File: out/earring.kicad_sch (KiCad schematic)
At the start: 51 parts, among them J1 USB-C, SW1 BOOTSEL, SW2 PWR, U1 RP2350A, U2 LGS4056H, U3 NCP730-3.3, U4 TPS22913, U5 USBLC6-2P6, U6 LSM6DS3TR-C, U7 W25Q16JVUXIQ, Y1 12MHz

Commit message: Link schematic to PCB: footprint properties, UUID paths, fp-lib-table
Fixes 'Cannot update <ref> (no footprint assigned)' on Update PCB from
Schematic. Four things were missing:

- Symbols had no Footprint property. Each now carries
  'earring:<footprint>' taken from bom/parts.yaml via circuit.py.
- No fp-lib-table, so that nickname resolved to nothing. gen_board.py
  writes out/fp-lib-table pointing at library/parts.pretty (tracked).
- Board footprints had bare FPIDs and empty paths, so KiCad could not
  tell that board R10 IS schematic R10. gen_board.py now stamps the
  library nickname and the schematic symbol's UUID path; both sides
  derive UUIDs deterministically, so neither has to run first.
- The project file listed no root sheet ('sheets': []).

The bigger fix: the schematic is now COMPLETE. The 45-LED chain and the
bypass-cap banks were collapsed to representatives plus a note, which
reads well but is wrong for a sheet that drives the board — KiCad
offers to DELETE any footprint with no matching symbol, so the 41
undrawn LEDs and 23 ring caps were at risk. They are drawn in full as
grids (page A2 -> A1), with an assert that every component is placed.
Unused pins get no-connect flags instead of dangling.

The existing PARTIAL board was patched in place, NOT regenerated:
1363 tracks before and after, DRC unchanged at 0 errors / 8 unconnected.

Verified: kicad-cli sch erc = 0 violations; netlist export = 122/122
components with footprints; cross-check of every board footprint
against its symbol = 0 path/footprint/orphan mismatches.

Co-Authored-By: Claude Fable 5 <noreply@anthropic.com>
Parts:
- added C2, C3, C30, C32, C34, C36, C38, C4, C40, C42, C44, C46, C48, C5, C50, C52, C54, C56, C58, C6, C60, C62, C64, C66, C68, C7, C70, C72, C74, C8: 100n, earring:C_0402_1005Metric, symbol gen:c_100n
- added LED10, LED11, LED12, LED13, LED14, LED15, LED16, LED17, LED18, LED19, LED20, LED21, LED22, LED23, LED24, LED25, LED26, LED27, LED28, LED29, LED3, LED30, LED31, LED32, LED33, LED34, LED35, LED36, LED37, LED38, LED39, LED4, LED40, LED41, LED42, LED43, LED5, LED6, LED7, LED8, LED9: SK6805-EC10, earring:LED_SK6805-EC10, symbol gen:led
- BT1: footprint (none) -> earring:BAT_CR2032_W
- C1, C14, C15, C18, C19, C21, C23, C24, C25, C9: footprint (none) -> earring:C_0402_1005Metric
- C11, C12, C13, C22: footprint (none) -> earring:C_0402_1005Metric_small_pads
- C16, C17, C20: footprint (none) -> earring:C_0603_1608Metric
- J1: footprint (none) -> earring:USB-C_SMD-TYPE-C-31-M-12_1
- L1: footprint (none) -> earring:L_pol_2016
- LED1, LED2, LED44, LED45: footprint (none) -> earring:LED_SK6805-EC10
- R1, R10, R11, R12, R13, R14, R15, R2, R3, R4, R5, R6, R7, R8: footprint (none) -> earring:R_0402_1005Metric
- SW1: footprint (none) -> earring:SW-SMD_L6.0-W3.3-LS8.0_TS-1101-C-W
- SW2: footprint (none) -> earring:SW-TH_MSK12C02
- TP1, TP2, TP3: footprint (none) -> earring:TestPoint_Pad_1.5x1.5mm
- U1: footprint (none) -> earring:RP2350-QFN-60-1EP_7x7_P0.4mm_EP3.4x3.4mm_ThermalVias
- U2: footprint (none) -> earring:DFN-8-1EP_2x2mm_P0.5mm_EP0.9x1.5mm
- U3: footprint (none) -> earring:WDFN-6-2x2
- U4: footprint (none) -> earring:YZV0004ADAD
- U5: footprint (none) -> earring:SOT-666
- U6: footprint (none) -> earring:LGA-14_L3.0-W2.5-P0.50-TL
- U7: footprint (none) -> earring:USON-8_L3.0-W2.0-P0.50-BL-EP
- Y1: footprint (none) -> earring:Crystal_SMD_2520-4Pin_2.5x2.0mm
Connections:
- net 3V3: now also C2.1, C3.1, C4.1, C5.1, C6.1, C7.1, C8.1
- net GND: now also C2.2, C3.2, C30.2, C32.2, C34.2, C36.2, C38.2, C4.2, C40.2, C42.2, C44.2, C46.2, C48.2, C5.2, C50.2, C52.2, C54.2, C56.2, C58.2, C6.2, C60.2, C62.2, C64.2, C66.2, C68.2, C7.2, C70.2, C72.2, C74.2, C8.2, LED10.1 (GND), LED11.1 (GND), LED12.1 (GND), LED13.1 (GND), LED14.1 (GND), LED15.1 (GND), LED16.1 (GND), LED17.1 (GND), LED18.1 (GND), LED19.1 (GND), LED20.1 (GND), LED21.1 (GND), LED22.1 (GND), LED23.1 (GND), LED24.1 (GND), LED25.1 (GND), LED26.1 (GND), LED27.1 (GND), LED28.1 (GND), LED29.1 (GND), LED3.1 (GND), LED30.1 (GND), LED31.1 (GND), LED32.1 (GND), LED33.1 (GND), LED34.1 (GND), LED35.1 (GND), LED36.1 (GND), LED37.1 (GND), LED38.1 (GND), LED39.1 (GND), LED4.1 (GND), LED40.1 (GND), LED41.1 (GND), LED42.1 (GND), LED43.1 (GND), LED5.1 (GND), LED6.1 (GND), LED7.1 (GND), LED8.1 (GND), LED9.1 (GND)
- net LED_D2: now also LED3.2 (DIN)
- net LED_D43: now also LED43.4 (DOUT)
- net VLED: now also C30.1, C32.1, C34.1, C36.1, C38.1, C40.1, C42.1, C44.1, C46.1, C48.1, C50.1, C52.1, C54.1, C56.1, C58.1, C60.1, C62.1, C64.1, C66.1, C68.1, C70.1, C72.1, C74.1, LED10.3 (VDD), LED11.3 (VDD), LED12.3 (VDD), LED13.3 (VDD), LED14.3 (VDD), LED15.3 (VDD), LED16.3 (VDD), LED17.3 (VDD), LED18.3 (VDD), LED19.3 (VDD), LED20.3 (VDD), LED21.3 (VDD), LED22.3 (VDD), LED23.3 (VDD), LED24.3 (VDD), LED25.3 (VDD), LED26.3 (VDD), LED27.3 (VDD), LED28.3 (VDD), LED29.3 (VDD), LED3.3 (VDD), LED30.3 (VDD), LED31.3 (VDD), LED32.3 (VDD), LED33.3 (VDD), LED34.3 (VDD), LED35.3 (VDD), LED36.3 (VDD), LED37.3 (VDD), LED38.3 (VDD), LED39.3 (VDD), LED4.3 (VDD), LED40.3 (VDD), LED41.3 (VDD), LED42.3 (VDD), LED43.3 (VDD), LED5.3 (VDD), LED6.3 (VDD), LED7.3 (VDD), LED8.3 (VDD), LED9.3 (VDD)
- new net LED_D10: LED10.4 (DOUT), LED11.2 (DIN)
- new net LED_D11: LED11.4 (DOUT), LED12.2 (DIN)
- new net LED_D12: LED12.4 (DOUT), LED13.2 (DIN)
- new net LED_D13: LED13.4 (DOUT), LED14.2 (DIN)
- new net LED_D14: LED14.4 (DOUT), LED15.2 (DIN)
- new net LED_D15: LED15.4 (DOUT), LED16.2 (DIN)
- new net LED_D16: LED16.4 (DOUT), LED17.2 (DIN)
- new net LED_D17: LED17.4 (DOUT), LED18.2 (DIN)
- new net LED_D18: LED18.4 (DOUT), LED19.2 (DIN)
- new net LED_D19: LED19.4 (DOUT), LED20.2 (DIN)
- new net LED_D20: LED20.4 (DOUT), LED21.2 (DIN)
- new net LED_D21: LED21.4 (DOUT), LED22.2 (DIN)
- new net LED_D22: LED22.4 (DOUT), LED23.2 (DIN)
- new net LED_D23: LED23.4 (DOUT), LED24.2 (DIN)
- new net LED_D24: LED24.4 (DOUT), LED25.2 (DIN)
- new net LED_D25: LED25.4 (DOUT), LED26.2 (DIN)
- new net LED_D26: LED26.4 (DOUT), LED27.2 (DIN)
- new net LED_D27: LED27.4 (DOUT), LED28.2 (DIN)
- new net LED_D28: LED28.4 (DOUT), LED29.2 (DIN)
- new net LED_D29: LED29.4 (DOUT), LED30.2 (DIN)
- new net LED_D3: LED3.4 (DOUT), LED4.2 (DIN)
- new net LED_D30: LED30.4 (DOUT), LED31.2 (DIN)
- new net LED_D31: LED31.4 (DOUT), LED32.2 (DIN)
- new net LED_D32: LED32.4 (DOUT), LED33.2 (DIN)
- new net LED_D33: LED33.4 (DOUT), LED34.2 (DIN)
- new net LED_D34: LED34.4 (DOUT), LED35.2 (DIN)
- new net LED_D35: LED35.4 (DOUT), LED36.2 (DIN)
- new net LED_D36: LED36.4 (DOUT), LED37.2 (DIN)
- new net LED_D37: LED37.4 (DOUT), LED38.2 (DIN)
- new net LED_D38: LED38.4 (DOUT), LED39.2 (DIN)
- new net LED_D39: LED39.4 (DOUT), LED40.2 (DIN)
- new net LED_D4: LED4.4 (DOUT), LED5.2 (DIN)
- new net LED_D40: LED40.4 (DOUT), LED41.2 (DIN)
- new net LED_D41: LED41.4 (DOUT), LED42.2 (DIN)
- new net LED_D42: LED42.4 (DOUT), LED43.2 (DIN)
- new net LED_D5: LED5.4 (DOUT), LED6.2 (DIN)
- new net LED_D6: LED6.4 (DOUT), LED7.2 (DIN)
- new net LED_D7: LED7.4 (DOUT), LED8.2 (DIN)
- new net LED_D8: LED8.4 (DOUT), LED9.2 (DIN)
- new net LED_D9: LED10.2 (DIN), LED9.4 (DOUT)
- no-connect marks 0 -> 30
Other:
- note added: "Connections are shown as GLOBAL NET LABELS, not wires — same-named labels are the same net. Every component is drawn, so this sheet can drive the PCB. Generated from scripts/circuit.py; do not hand-edit."
- note added: "LED ring bypass caps — one per 2 LEDs, VLED-GND [23]"
- note added: "LED ring — SK6805-EC10 chain (DOUT n -> DIN n+1 = LED_D<n>; head LED_D0 from U1; VDD = VLED) [45]"
- note added: "MCU decoupling — 3V3-GND, one per IOVDD/OTP_VDD/QSPI_IOVDD/ADC_AVDD pin [8]"
- note removed: "45 LEDs total: 34 on the perimeter + 3 tip chevron + 8 interior. DOUT(n) -> DIN(n+1) as LED_D<n>; chain head LED_D0 comes from U1. VDD = VLED (switched"
- note removed: "Connections are shown as GLOBAL NET LABELS, not wires — same-named labels are the same net. Generated from scripts/circuit.py; do not hand-edit."
- note removed: "Decoupling (MCU cluster)"
- note removed: "LED ring — SK6805-EC10 addressable chain"
- note removed: "Not drawn individually (all present on the board and in the BOM): C30..C74 (23); LED3..LED43 (41)"
- note removed: "VBATT via U4), GND common. 23 x 100n bypass caps ride the ring (one per 2 LEDs): C30..C74, each VLED-GND."
- note removed: "x9 in parallel 3V3-GND: C1, C2, C3, C4, C5, C6, C7, C8, C9 — one per IOVDD/OTP_VDD/QSPI_IOVDD/ADC_AVDD pin."
- note removed: "··· LED3..LED43 (41 more, identical) ···"
- moved on the sheet: C1, LED1, LED2, LED44, LED45

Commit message: Save latest PCB/schematic edits from KiCad; add BOOTSEL switch 3D model
Hand-routing progress on out/earring.kicad_pcb plus KiCad's resave of the
schematic and project file. Adds parts/ with the WRL model for the
KEY-SMD_4P-L4.2-W3.2-P2.20-LS4.6 tactile switch.

Co-Authored-By: Claude Fable 5 <noreply@anthropic.com>
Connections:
- net USB_DM renamed USB_DN

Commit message: BOOTSEL: swap TS-1101-C-W for SKRPAME010 (C19724063), 4-pin tact
Smaller part: pads move from (+-3.70, 0) to (+-2.10, +-1.07), body
4.2x3.2mm vs 6.0x3.3mm. Footprint pulled via easyeda2kicad into
library/parts.pretty; 3D model is the vendor WRL in parts/ with the
mm -> 0.1in scale (x0.3937) BAKED INTO ITS VERTICES, so the footprint
keeps (scale 1 1 1) -- KiCad's scale field has export issues.

circuit.py: SW1 is now 4 pads, 1-2 = BOOTSEL_SW and 3-4 = GND (per the
LCSC symbol; confirm against the ALPS drawing before ordering).
Schematic regenerated. PCB footprint swapped in place via pcbnew,
keeping position, rotation, reference and the schematic UUID path;
Sequoia rerouted the CC1/CC2 collisions the new pad positions caused.

DRC: 3 errors left, all on the LED ring (VLED via shorting the LED_D41
arc), none from SW1. 0 unconnected.

Co-Authored-By: Claude Fable 5 <noreply@anthropic.com>
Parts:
- added J6: SM03B-SRSS-TB, Connector_JST:JST_SH_BM03B-SRSS-TB_1x03-1MP_P1.00mm_Vertical, symbol Connector_Generic_MountingPin:Conn_01x03_MountingPin
- SW1: footprint earring:SW-SMD_L6.0-W3.3-LS8.0_TS-1101-C-W -> earring:KEY-SMD_4P-L4.2-W3.2-P2.20-LS4.6
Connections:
- net BOOTSEL_SW: now also SW1.2
- net GND: now also SW1.3, SW1.4, J6.2 (Pin_2), J6.MP (MountPin); no longer SW1.2
- net SWCLK: now also J6.1 (Pin_1)
- net SWDIO: now also J6.3 (Pin_3)
- net USB_DN renamed USB_DM
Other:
- note added: "JST Debug Connector"
- moved on the sheet: C14, C15, R1, Y1

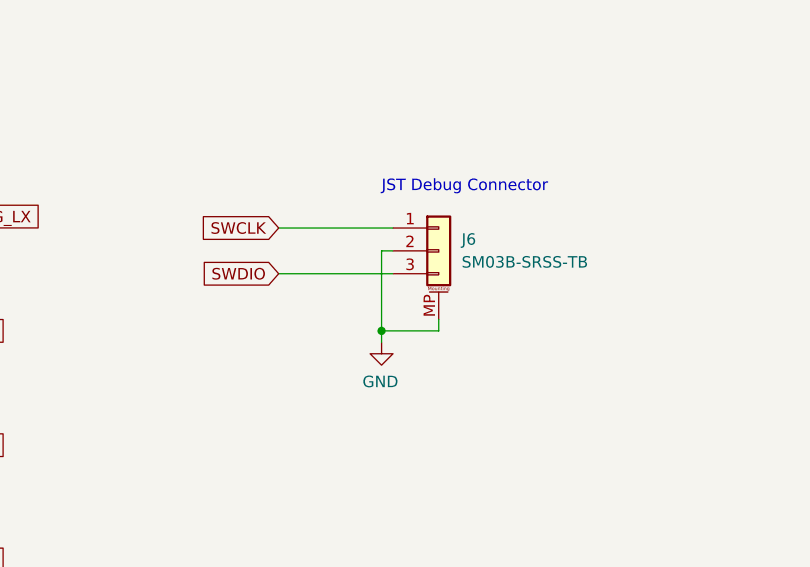
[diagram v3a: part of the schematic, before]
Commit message: BOM: r_4k7 C25900 -> C105871 (in stock)
C25900 (UNI-ROYAL 0402WGF4701TCE) is out of stock at LCSC. C105871 is
YAGEO RC0402FR-074K7L -- same 4.7k 1% 0402, 5.5M in stock, available for
JLC SMT assembly, and the same YAGEO RC0402 series already used for r_27.
Board LCSC fields on R14/R15 resynced to match.

Co-Authored-By: Claude Fable 5 <noreply@anthropic.com>
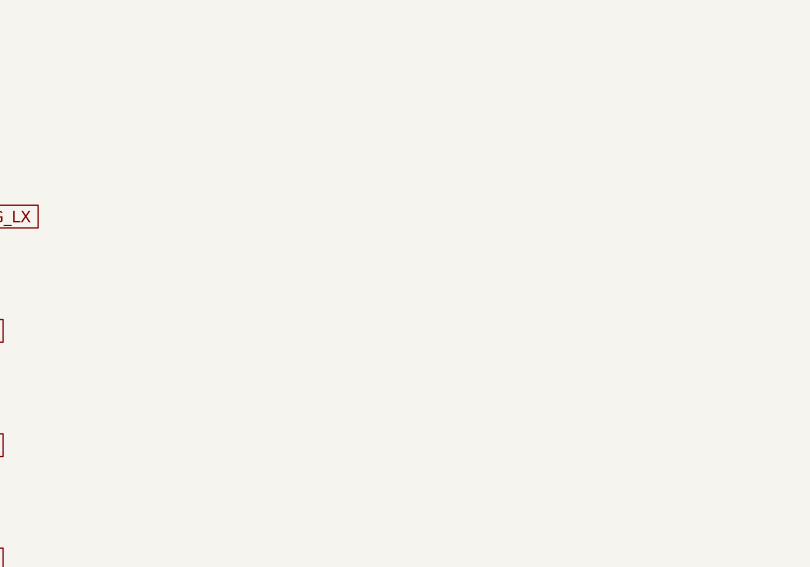
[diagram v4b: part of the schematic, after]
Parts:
- removed J6: SM03B-SRSS-TB, Connector_JST:JST_SH_BM03B-SRSS-TB_1x03-1MP_P1.00mm_Vertical, symbol Connector_Generic_MountingPin:Conn_01x03_MountingPin
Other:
- note removed: "JST Debug Connector"

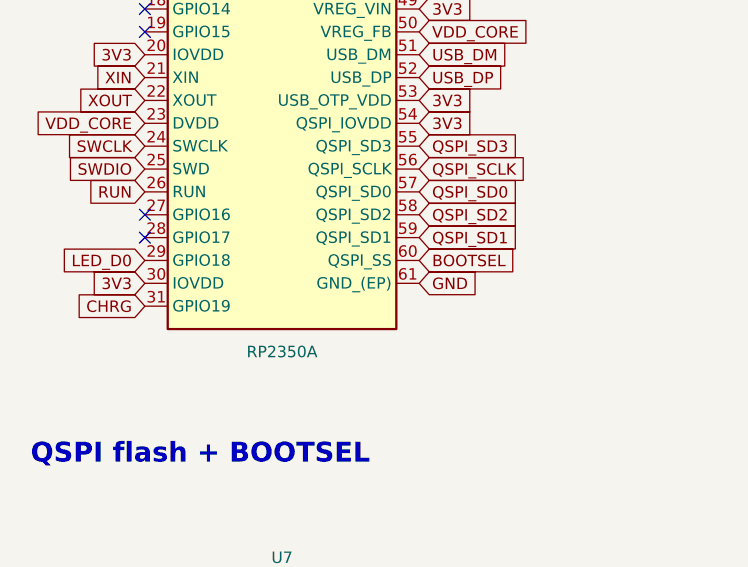
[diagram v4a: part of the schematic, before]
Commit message: Crystal: swap to Abracon ABM8-272-T3 (C20625731), the RP2350-recommended part
JLCPCB's notice ("does not use the recommended crystal and polarised
inductor circuitry") was about the crystal -- the inductor was already
correct. Was C284155 (Yajingxin, 2520): CL 12pF, max ESR 120R. But C14/C15
(15p) and R1 (1k) were copied from the RP2350 hardware design guide, which
derives them for a CL 10pF / ESR<=50R crystal -- 15p/2 + 3p stray = 10.5pF,
and 1k is sized not to over-drive a <=50R part at 3.3V IOVDD. Against a
12pF/120R crystal the caps ran it fast and the 1k ate cold-start margin.

Swapping the crystal (rather than retuning to 18p + a smaller R) makes the
existing 15p/1k correct again and matches the part Pico 2 was tuned for. A
drop-in 2520 was not available: at 12MHz the smaller blank runs ~100R+ ESR,
which is why RPi chose a 3225.

Land pattern copied exactly from the official RPI-RP2350A-MINIMAL R4 board
in docs/ (generic_xtalcc320x250x80-4): pads 1.4x1.2 at (+-1.1, +-0.85).
Pin convention is unchanged (1/3 crystal, 2/4 GND) so pad nets carried over
by number -- the swap script asserts this rather than assuming it.

Board was 0 errors before this; now 21, ALL touching Y1 or C14, 0
unconnected. The land grew 0.35mm/side in x and 0.25mm in y, so XIN/XOUT
and a RUN via now foul the pads and C14 overlaps the courtyard. Needs a
hand repack of the crystal pocket.

Co-Authored-By: Claude Fable 5 <noreply@anthropic.com>
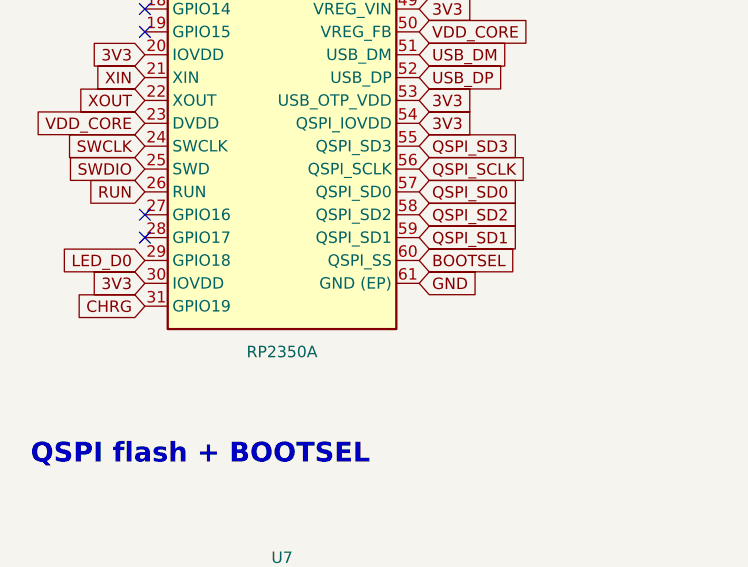
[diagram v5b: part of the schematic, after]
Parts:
- Y1: footprint earring:Crystal_SMD_2520-4Pin_2.5x2.0mm -> earring:Crystal_SMD_3225-4Pin_3.2x2.5mm_ABM8

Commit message: Datasheet review of every chip: two fatal pinout bugs fixed
Read each IC's primary datasheet (figures included) rather than trusting
symbols or prior boards, and diffed the RP2350A against Raspberry Pi's own
RPI-RP2350A-MINIMAL R4 project in docs/. Full write-up in
docs/REVIEW-2026-08-06.md.

Two errors would have killed the board:

* U6 LSM6DS3TR-C serial pins were rotated by one. ST Table 2 / Figure 1
  (DocID030071 rev 3) give 12=CS, 13=SCL, 14=SDA; circuit.py had
  12=SCL, 13=SDA, 14=CS. As built, CS was driven by the I2C clock (so the
  part re-entered SPI mode on every edge) and SDA -- open-drain -- was
  strapped hard to 3V3, shorting the rail through the IMU's output FET
  whenever it tried to ACK. The footprint numbering was verified correct
  against Figure 1; only the netlist was wrong.

* SW1 SKRPAME010 shorted BOOTSEL_SW to GND. The footprint puts pads 1/3 on
  one side of the body and 2/4 on the other, so the SPST contacts are the
  same-side pairs {1,3} and {2,4}, not {1,2}/{3,4}. Netting both pads of an
  assumed pair tied both nets to both contacts, which would have held
  QSPI_SS low and booted to the USB bootloader forever. Now netted on the
  diagonal only (1=BOOTSEL_SW, 4=GND, 2/3 unnetted), which is correct under
  either pairing convention.

Also:
* VDD_CORE had no HF decoupling (ds 6.1.3 wants 100n on the two DVDD pins
  nearest the regulator). No room for new 0402s, but C5/C6 already sat
  1.39/1.63mm from DVDD 39/6 -- they move from 3V3 to VDD_CORE. IOVDD 38/1
  share with C3/C4, the trade RPi's guide 2.2.1 documents making.
* C28: 100n at the USBLC6-2P6, which ST's ds section 3 asks for so VBUS is
  a stiff clamp reference. Placed on B.Cu 3.2mm from U5.

gen_schematic.py gains a fifth honesty check: check_text() refuses to emit
a sheet where any reference, value or note lands on a wire or on other
text. It found 20 real clashes on the existing sheet; placement rules now
derive the free side from where each part's pins actually point after
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
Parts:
- added C28: 100n, earring:C_0402_1005Metric, symbol gen:C
- BT1: symbol gen:battery_clip -> gen:BATT
- C1, C2, C21, C23, C24, C25, C3, C30, C32, C34, C36, C38, C4, C40, C42, C44, C46, C48, C5, C50, C52, C54, C56, C58, C6, C60, C62, C64, C66, C68, C7, C70, C72, C74, C8, C9: symbol gen:c_100n -> gen:C
- C11, C12, C13, C22: symbol gen:c_4u7 -> gen:C
- C14, C15: symbol gen:c_15p -> gen:C
- C16, C17, C20: symbol gen:c_10u_0603 -> gen:C
- C18, C19: symbol gen:c_1u -> gen:C
- L1: symbol gen:vreg_inductor -> gen:L
- R1, R3: symbol gen:r_1k -> gen:R
- R10, R2: symbol gen:r_10k -> gen:R
- R11, R12: symbol gen:r_1m -> gen:R
- R13: symbol gen:r_33 -> gen:R
- R14, R15: symbol gen:r_4k7 -> gen:R
- R4, R5: symbol gen:r_5k1 -> gen:R
- R6, R7: symbol gen:r_27 -> gen:R
- R8: symbol gen:r_22k -> gen:R
- SW1: symbol gen:bootsel_button -> gen:SW_PUSH
- SW2: symbol gen:slide_switch -> gen:SW_SPDT
- TP1, TP2, TP3: symbol gen:testpoint -> gen:TP
- Y1: symbol gen:crystal -> gen:XTAL
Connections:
- net 3V3: now also U6.12 (CS); no longer C5.1, C6.1, U6.14 (SDA)
- net BOOTSEL_SW: no longer SW1.2
- net GND: now also C28.2; no longer SW1.3
- net IMU_SCL: now also U6.13 (SCL); no longer U6.12 (INT2)
- net IMU_SDA: now also U6.14 (SDA); no longer U6.13 (SCL)
- net VBUS: now also C28.1
- net VDD_CORE: now also C5.1, C6.1
- no-connect marks 30 -> 32
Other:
- note added: "0x6A."
- note added: "123 components / 81 nets / 4-layer JLCPCB stackup. Power rails (GND, 3V3, VBATT, VLED, VBUS, VDD_CORE) are power symbols; only cross-block signals use global labels. Generated from scripts/circuit.py — do not hand-edit; rebuild with `python3 build.py --only schematic`."
- note added: "12MHz crystal"
- note added: "1M:1M divider -> half VBATT, filtered; read on"
- note added: "3V3 LDO + power slide switch (switches EN, not the cell)"
- note added: "ABM8-272-T3, CL 10pF / ESR<=50R — the 15p caps and R1 are matched to it;"
- note added: "Addressable LED ring — 45 x SK6805-EC10 daisy chain"
- note added: "Battery voltage sense -> ADC"
- note added: "C30..C74, distributed around the ring next to their LEDs"
- note added: "CHRG / DONE are open-drain -> GPIO with internal pull-up (low = active); software owns the charge indicator."
- note added: "CS/SDx/SCx -> VDDIO selects I2C mode 1 and idles the aux master; SDO/SA0 -> GND sets address"
- note added: "Chain runs LED1 -> LED45 in board order; each row break carries on through LED_D<n>. VLED is the switched battery rail, so the ring is dark until LED_EN goes high."
- note added: "GPIO29/ADC3."
- note added: "IMU — LSM6DS3TR-C on I2C1 (addr 0x6A)"
- note added: "IOVDD 38 and 1 share with C3/C4 — C5/C6 went to the core rail (see the regulator block)"
- note added: "J1 is a TYPE-C-31-M-12 right-angle receptacle. VBUS is charge-only: there is no"
- note added: "L1 dot on the VOUT (pad 1) side — ds Fig 23. C11 CIN; C12 COUT at"
- note added: "L1; C13 the 2nd 4u7 at DVDD 23 (§6.3.8.1). C5/C6 are the 100n HF"
- note added: "LED ring bypass — 100n VLED-GND, one per two LEDs"
- note added: "Li-ion charger (LGS4056H, ~41mA) + LIR2032 cell"
- note added: "MCU decoupling — 100n on the 3V3 supply pins"
- note added: "Pico-style: QSPI_SS is both the flash /CS and the BOOTSEL strap."
- note added: "QSPI flash (BOOTSEL strap on /CS)"
- note added: "R10 holds the switch off until firmware drives LED_EN high."
- note added: "RP2350 core buck regulator (ds §6.3.8)"
- note added: "RP2350A"
- note added: "RUN / SWD"
- note added: "USB-C receptacle / ESD / series R"
- note added: "VBUS->3V3 path, the MCU always runs from the cell."
- note added: "VLED high-side load switch (LEDs draw zero when off)"
- note added: "do not retune."
- note added: "pair §6.1.3 wants on the two DVDD pins nearest the regulator —"
- note added: "simple_earring — generated schematic"
- note added: "they already sat there, netted to 3V3. R13+C22 filter VREG_AVDD."
- note removed: "122 components / 81 nets / 4-layer stackup / MCU RP2350A + W25Q16JV QSPI flash / 45 x SK6805-EC10"
- note removed: "3V3 LDO + power switch"
- note removed: "Charger + battery"
- note removed: "Connections are shown as GLOBAL NET LABELS, not wires — same-named labels are the same net. Every component is drawn, so this sheet can drive the PCB. Generated from scripts/circuit.py; do not hand-edit."
- note removed: "Crystal"
- note removed: "Debug / test points"
- note removed: "IMU (I2C1)"
- note removed: "LED ring bypass caps — one per 2 LEDs, VLED-GND [23]"
- note removed: "LED ring — SK6805-EC10 chain (DOUT n -> DIN n+1 = LED_D<n>; head LED_D0 from U1; VDD = VLED) [45]"
- note removed: "MCU"
- note removed: "MCU decoupling — 3V3-GND, one per IOVDD/OTP_VDD/QSPI_IOVDD/ADC_AVDD pin [8]"
- note removed: "QSPI flash + BOOTSEL"
- note removed: "RP2350 core regulator"
- note removed: "USB-C + ESD + series R"
- note removed: "VLED load switch"
- note removed: "simple_earring — generated schematic (regenerate: python3 build.py --only schematic)"
- moved on the sheet: BT1, J1, LED1, LED10, LED11, LED12, LED13, LED14, LED15, LED16, LED17, LED18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
